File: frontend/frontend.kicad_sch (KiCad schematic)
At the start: 49 parts, among them Q1 T2N7002AK,LM, Q2 NX3008PBK,215, Q3 NX3008PBK,215, Q4 T2N7002AK,LM, Q5 NX3008PBK,215, Q6 T2N7002AK,LM, U1 ADS1291/2, U2 KC2016Z2

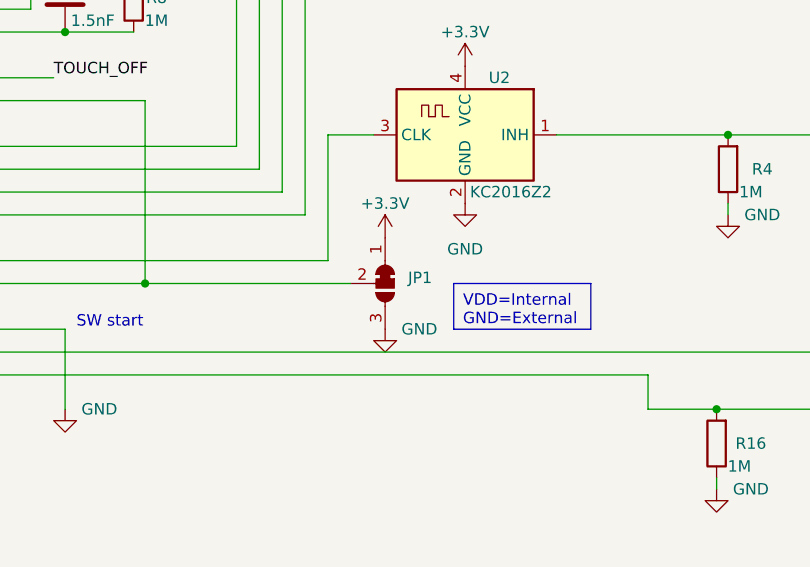
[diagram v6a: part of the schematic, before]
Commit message: Tweak frontend routing
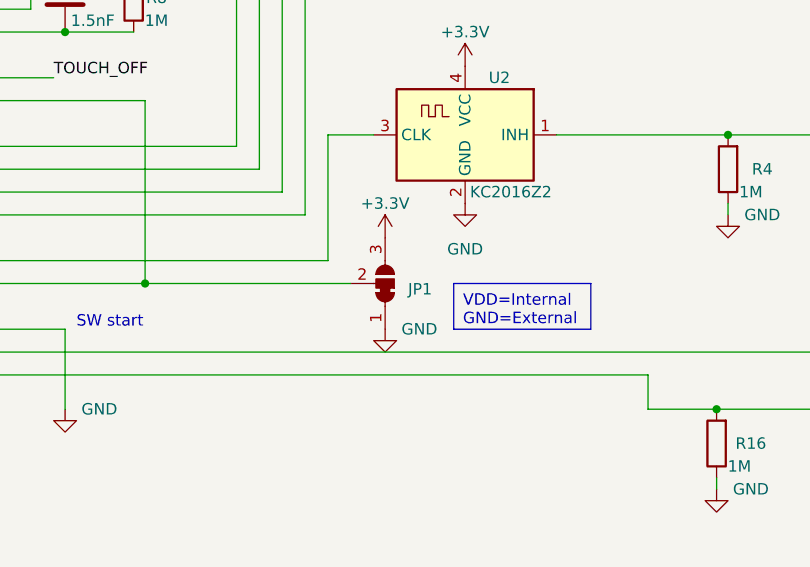
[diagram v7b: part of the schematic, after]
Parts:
- JP1: footprint Jumper:SolderJumper-3_P1.3mm_Open_RoundedPad1.0x1.5mm -> Jumper:SolderJumper-3_P1.3mm_Bridged12_RoundedPad1.0x1.5mm
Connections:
- net +3.3V: now also JP1.3 (B); no longer JP1.1 (A)
- net GND: now also JP1.1 (A); no longer JP1.3 (B)
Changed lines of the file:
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@@
     )
   )
-  (symbol (lib_id "Jumper:SolderJumper_3_Bridged12") (at 207.01 132.08 270) (unit 1)
-    (in_bom yes) (on_board yes) (dnp no) (fields_autoplaced)
-    (property "Reference" "JP1" (at 209.55 131.445 90)
+  (symbol (lib_id "Jumper:SolderJumper_3_Bridged12") (at 207.01 132.08 270) (mirror x) (unit 1)
+    (in_bom yes) (on_board yes) (dnp no)
+    (property "Reference" "JP1" (at 209.55 132.715 90)
       (effects (font (size 1.27 1.27)) (justify left))
     )
-    (property "Value" "SolderJumper_3_Bridged12" (at 209.55 133.985 90)
+    (property "Value" "SolderJumper_3_Bridged12" (at 209.55 130.175 90)
       (effects (font (size 1.27 1.27)) (justify left) hide)
     )
-    (property "Footprint" "Jumper:SolderJumper-3_P1.3mm_Open_RoundedPad1.0x1.5mm" (at 207.01 132.08 0)
+    (property "Footprint" "Jumper:SolderJumper-3_P1.3mm_Bridged12_RoundedPad1.0x1.5mm" (at 207.01 132.08 0)
       (effects (font (size 1.27 1.27)) hide)
     )

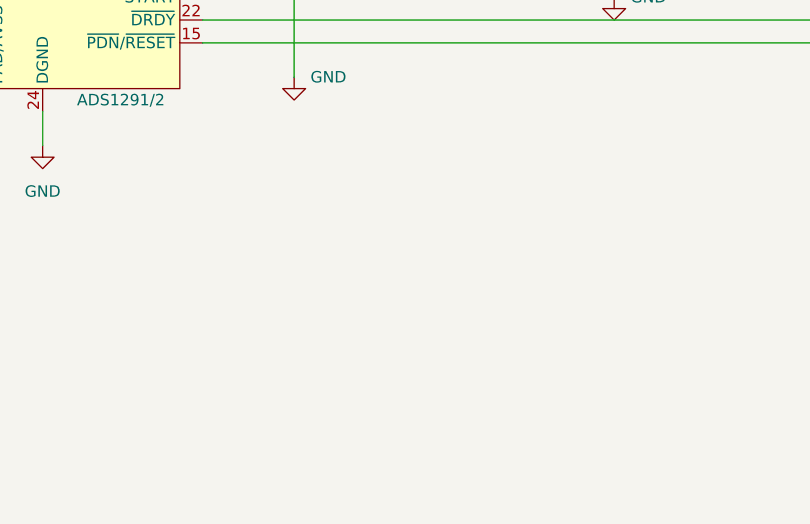
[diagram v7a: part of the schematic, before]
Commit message: Add logo to daughter board
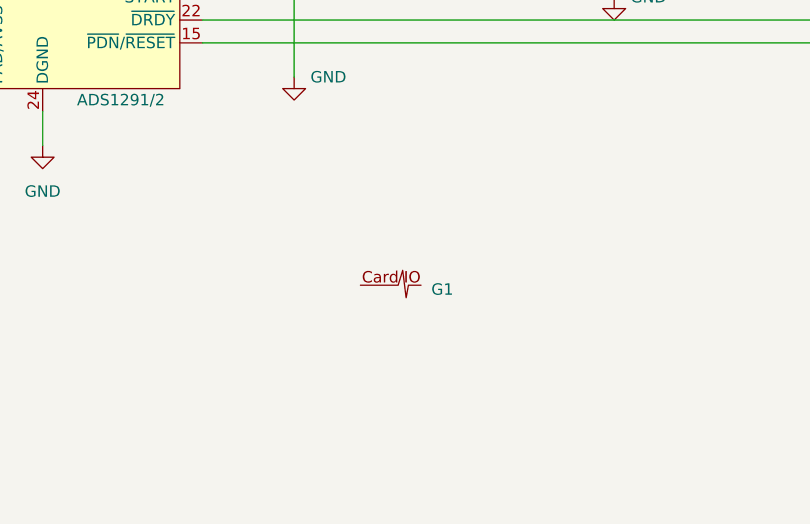
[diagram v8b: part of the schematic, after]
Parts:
- added G1: ~, frontend_parts:logo, symbol frontend_parts:logo
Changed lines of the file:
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@@
   (title_block
     (title "Card/IO ECG daughter board")
-    (date "2023-05-19")
+    (date "2023-06-04")
     (rev "2")
   )
@@
         )
       )
+    )
+  )
+  (symbol (lib_id "frontend_parts:logo") (at 182.245 168.91 0) (unit 1)
+    (in_bom yes) (on_board yes) (dnp no) (fields_autoplaced)
+    (property "Reference" "G1" (at 186.69 169.6362 0)
+      (effects (font (size 1.27 1.27)) (justify left))
+    )
+    (property "Value" "~" (at 182.245 168.91 0)
+      (effects (font (size 1.27 1.27)))
+    )
+    (property "Footprint" "frontend_parts:logo" (at 182.245 168.91 0)
+      (effects (font (size 1.27 1.27)) hide)
+    )
+    (property "Datasheet" "" (at 182.245 168.91 0)
+      (effects (font (size 1.27 1.27)) hide)
+    )
+    (instances
+      (project "frontend"
+        (path "/e7afbd42-f5d0-401b-b125-21ade79cd152"
+          (reference "G1") (unit 1)
+        )
+      )
